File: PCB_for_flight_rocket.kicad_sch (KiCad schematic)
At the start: 18 parts, among them U2 A000005, U5 LM1117T-3.3, U6 MC34063AP

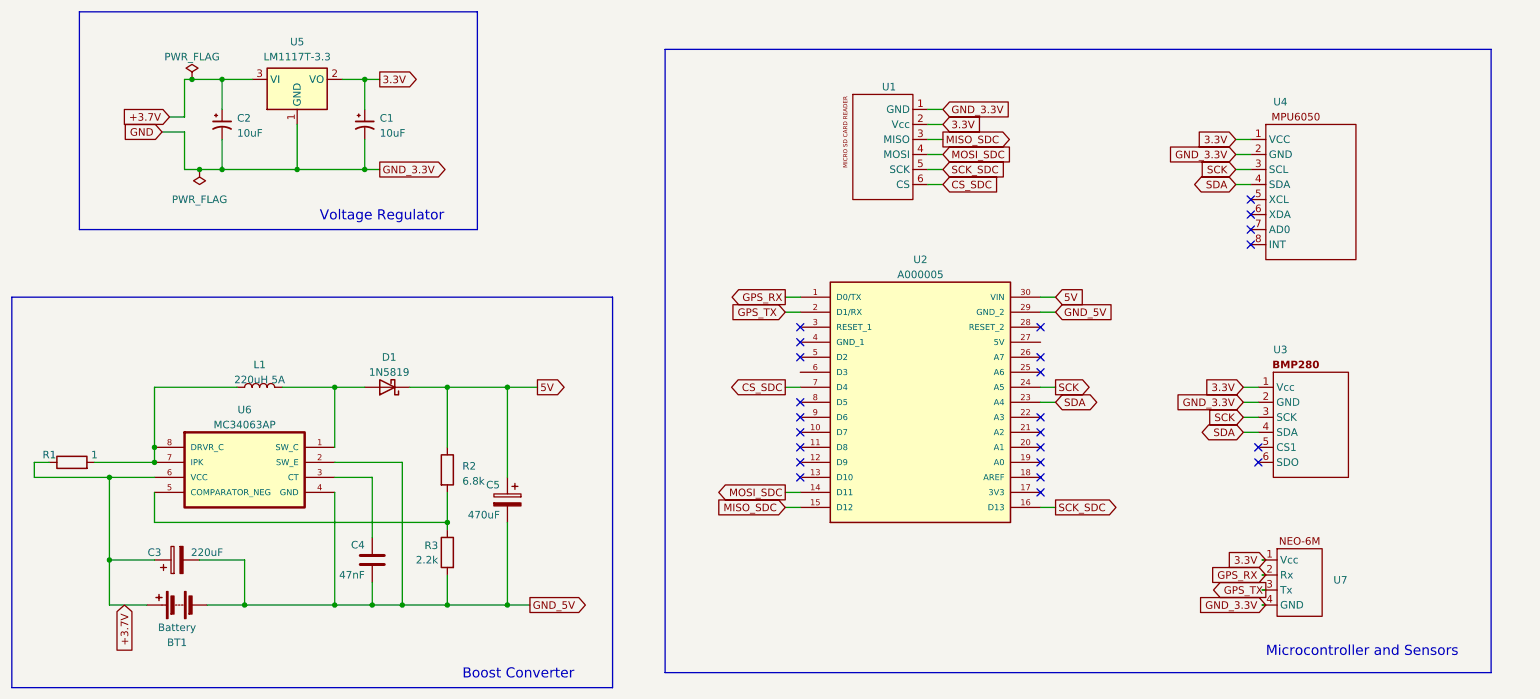
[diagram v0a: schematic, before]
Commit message: Added ground plane
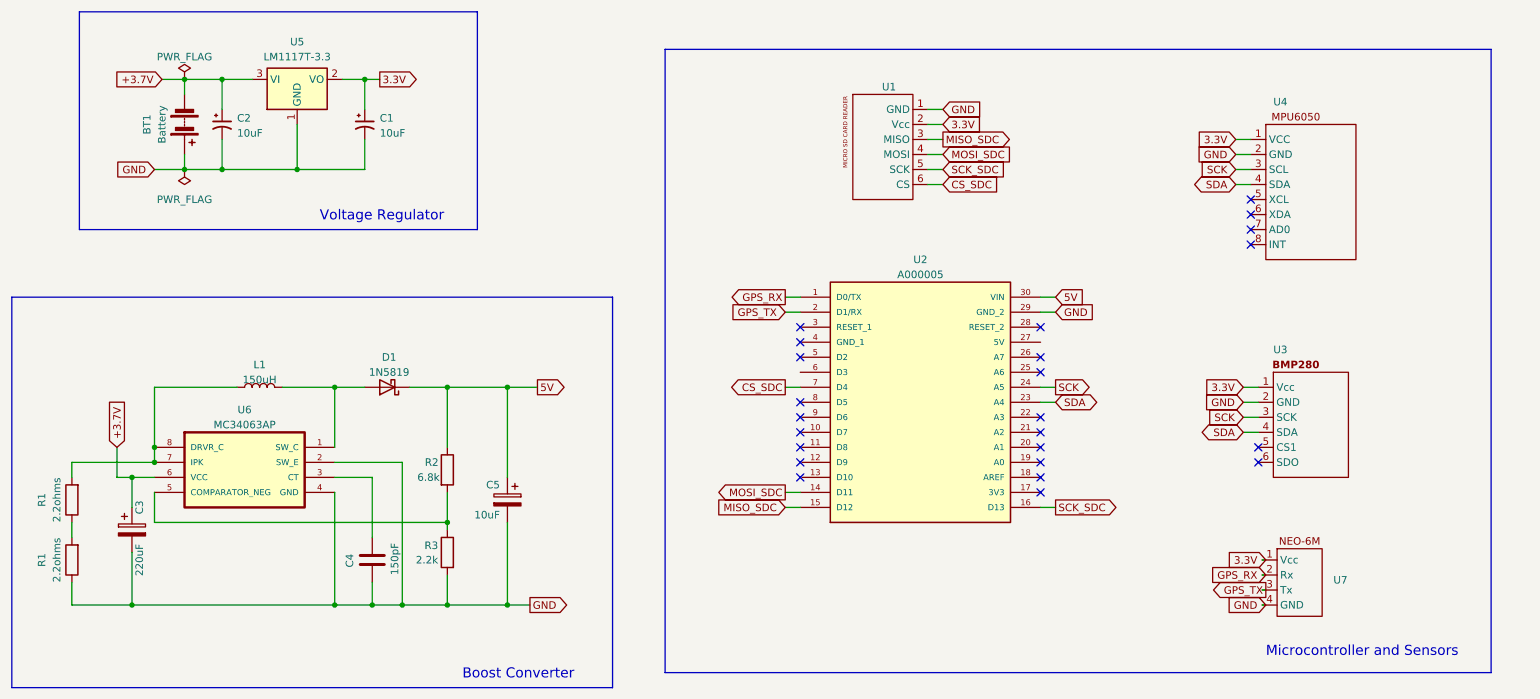
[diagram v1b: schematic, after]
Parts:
- added R1: 2.2ohms, Resistor_THT:R_Axial_DIN0207_L6.3mm_D2.5mm_P7.62mm_Horizontal, symbol Device:R
- C4: value 47nF -> 150pF
- C5: value 470uF -> 10uF; footprint lib:Capacitor_470uF -> lib:capacitor_10uF
- L1: value 220uH 5A -> 150uH; footprint lib:inductor_220uH -> Inductor_SMD:L_10.4x10.4_H4.8
- R1: value 1 -> 2.2ohms; footprint lib:resistor_1k -> Resistor_THT:R_Axial_DIN0207_L6.3mm_D2.5mm_P7.62mm_Horizontal
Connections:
- net +3.7V: now also BT1.2 (-); no longer BT1.1 (+), R1.1
- net GND: now also BT1.1 (+), C3.2, C4.2, C5.2, R3.2, U2.29 (GND_2), U6.2 (SW_E), U6.4 (GND), R1.1
- removed net GND_5V: BT1.2 (-), C3.2, C4.2, C5.2, R3.2, U2.29 (GND_2), U6.2 (SW_E), U6.4 (GND)
- new net: R1.1, R1.2
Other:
- moved on the sheet: BT1, C3, R1
